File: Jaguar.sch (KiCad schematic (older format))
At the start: 26 parts, among them P1 12v-SW, P10 TPS, P11 TPS-GND, P12 O2, P13 O2-GND, P14 CRANK-IN, P15 CAM-IN, P16 GND, P17 GND2, P18 DIS-BYPASS, P19 IGN-ADVANCE, P2 12v-SW2, P20 PT3-5, P21 Inj-IN, P22 INJ-GND, P23 12v-SW4, P24 RELAY-GND, P25 FUEL-, P26 Injectors, P3 12v-SW3, P4 BRV-12v, P5 Ground, P6 IAT, P7 MAT, P8 COOLANT, P9 Ground

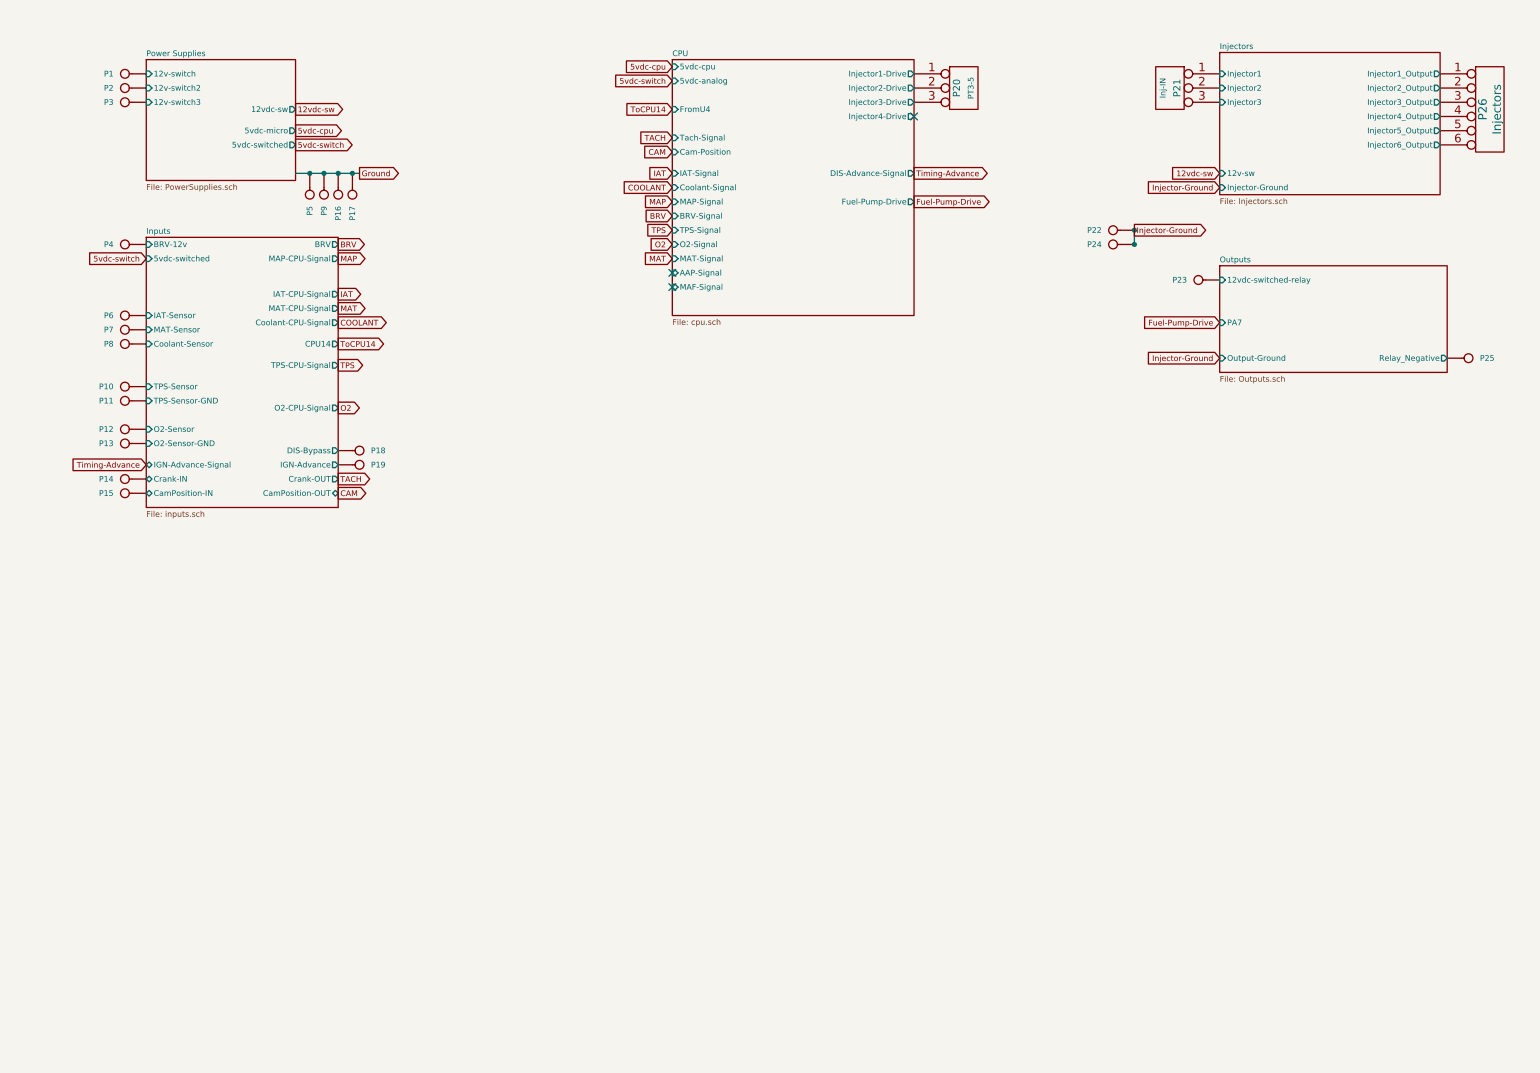
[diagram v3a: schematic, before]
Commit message: Improved schematic, re-design board, re-created PDF
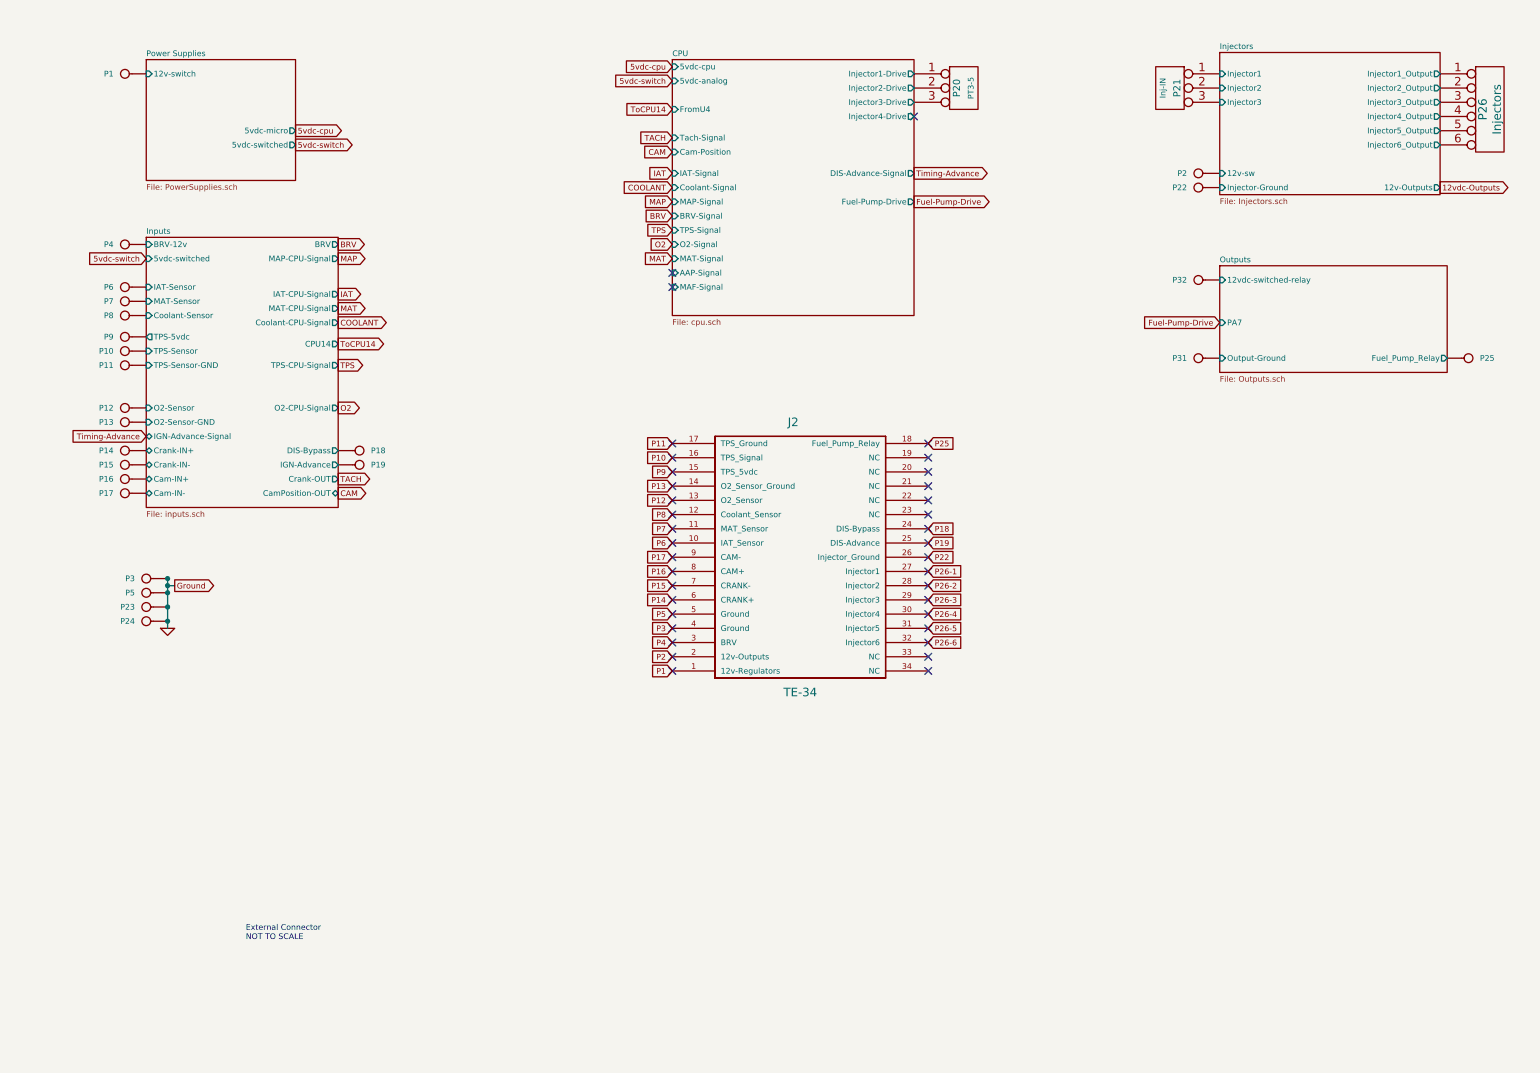
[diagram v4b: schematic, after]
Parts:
- added J2: TE-34, symbol TE-34
- added P31: OUT-GND, symbol CONN_1
- added P32: OUT-12v, symbol CONN_1
- P14: value CRANK-IN -> CRANK+
- P15: value CAM-IN -> CRANK-
- P16: value GND -> CAM+
- P17: value GND2 -> CAM-
- P23: value 12v-SW4 -> CRANK-GND
- P24: value RELAY-GND -> CAM-GND
- P3: value 12v-SW3 -> GND
- P5: value Ground -> GND2
- P9: value Ground -> TPS-5v
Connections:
- net labels added: 12vdc-Outputs, GND, P1, P10, P11, P12, P13, P14, P15, P16, P17, P18, P19, P2, P22, P25, P26-1, P26-2, P26-3, P26-4, P26-5, P26-6, P3, P4, P5, P6, P7, P8, P9
- net labels removed: 12vdc-sw, Injector-Ground
- no-connect marks 3 -> 37
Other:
- note added: "External Connector\nNOT TO SCALE"
- moved on the sheet: P10, P11, P12, P13, P14, P15, P16, P17, P2, P22, P3, P5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

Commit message: Fix MAX9926 Configuration and created new PCB and PDF
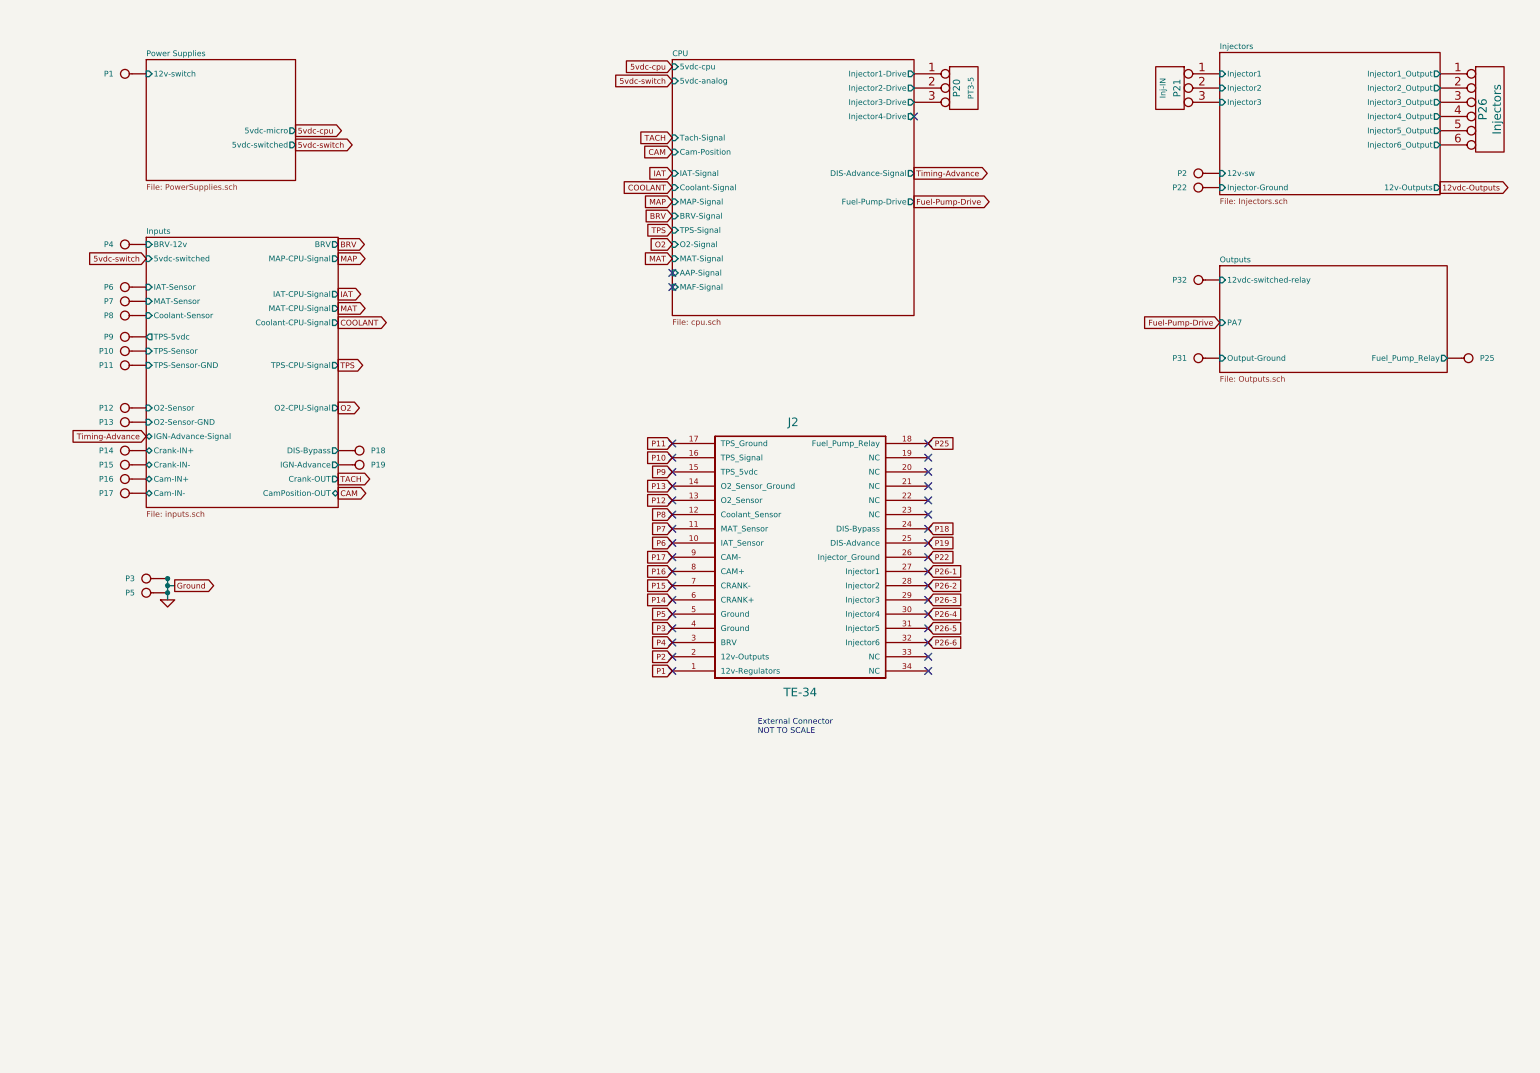
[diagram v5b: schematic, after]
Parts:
- removed P23: CRANK-GND, symbol CONN_1
- removed P24: CAM-GND, symbol CONN_1
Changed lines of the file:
@@
-EESchema Schematic File Version 2  date Mon 23 Jan 2012 07:28:42 AM EST
+EESchema Schematic File Version 2  date Mon 23 Jan 2012 01:49:16 PM EST
 LIBS:power
 LIBS:device
@@
 Comment4 ""
 $EndDescr
+Wire Wire Line
+	1650 4350 1650 4500
+Connection ~ 1650 4350
+Connection ~ 1650 4450
+Wire Wire Line
+	1700 4400 1650 4400
+Connection ~ 1650 4400
+$Sheet
+S 5200 700  1700 1800
+U 4F0A2F06
+F0 "CPU" 40
+F1 "cpu.sch" 40
+F2 "Fuel-Pump-Drive" O R 6900 1700 40
+F3 "Injector4-Drive" O R 6900 1100 40
+F4 "Injector3-Drive" O R 6900 1000 40
+F5 "Injector2-Drive" O R 6900 900 40
+F6 "Injector1-Drive" O R 6900 800 40
+F7 "DIS-Advance-Signal" O R 6900 1500 40
+F8 "Tach-Signal" I L 5200 1250 40
+F9 "MAF-Signal" I L 5200 2300 40
+F10 "MAT-Signal" I L 5200 2100 40
+F11 "BRV-Signal" I L 5200 1800 40
+F12 "MAP-Signal" I L 5200 1700 40
+F13 "O2-Signal" I L 5200 2000 40
+F14 "TPS-Signal" I L 5200 1900 40
+F15 "Coolant-Signal" I L 5200 1600 40
+F16 "IAT-Signal" I L 5200 1500 40
+F17 "AAP-Signal" I L 5200 2200 40
+F18 "Cam-Position" I L 5200 1350 40
+F19 "5vdc-analog" I L 5200 850 40
+F20 "5vdc-cpu" I L 5200 750 40
+$EndSheet
 $Comp
 L CONN_1 P32
@@
 F 1 "OUT-GND" H 8900 2855 30  0001 C CNN
 	1    8900 2800
-	-1   0    0    1
-$EndComp
-Connection ~ 1650 4650
-Connection ~ 1650 4550
-Wire Wire Line
-	1650 4700 1650 4350
-Connection ~ 1650 4400
-Wire Wire Line
-	1700 4400 1650 4400
-Connection ~ 1650 4450
-Connection ~ 1650 4350
-$Comp
-L CONN_1 P24
-U 1 1 4F1CCB30
-P 1500 4650
-F 0 "P24" H 1580 4650 40  0000 L CNN
-F 1 "CAM-GND" H 1500 4705 30  0001 C CNN
-	1    1500 4650
-	-1   0    0    1
-$EndComp
-$Comp
-L CONN_1 P23
-U 1 1 4F1CCB2B
-P 1500 4550
-F 0 "P23" H 1580 4550 40  0000 L CNN
-F 1 "CRANK-GND" H 1500 4605 30  0001 C CNN
-	1    1500 4550
 	-1   0    0    1
 $EndComp
@@
 L GND #PWR01
 U 1 1 4F1CCA54
-P 1650 4700
-F 0 "#PWR01" H 1650 4700 30  0001 C CNN
-F 1 "GND" H 1650 4630 30  0001 C CNN
-	1    1650 4700
+P 1650 4500
+F 0 "#PWR01" H 1650 4500 30  0001 C CNN
+F 1 "GND" H 1650 4430 30  0001 C CNN
+	1    1650 4500
 	1    0    0    -1
 $EndComp
@@
 Text GLabel 5200 5000 0    40   Input ~ 0
 P1
-Text Notes 2200 6900 0    40   ~ 0
+Text Notes 5800 5450 0    40   ~ 0
 External Connector\nNOT TO SCALE
 $Comp
@@
 F21 "CamPosition-OUT" B R 2850 3750 40
 F22 "Crank-OUT" O R 2850 3650 40
-F23 "CPU14" O R 2850 2700 40
-F24 "Cam-IN-" B L 1500 3750 40
-F25 "Crank-IN-" B L 1500 3550 40
-F26 "Cam-IN+" B L 1500 3650 40
-F27 "Crank-IN+" B L 1500 3450 40
-F28 "TPS-5vdc" O L 1500 2650 40
+F23 "Cam-IN-" B L 1500 3750 40
+F24 "Crank-IN-" B L 1500 3550 40
+F25 "Cam-IN+" B L 1500 3650 40
+F26 "Crank-IN+" B L 1500 3450 40
+F27 "TPS-5vdc" O L 1500 2650 40
 $EndSheet
 Text GLabel 1500 2100 0    40   Input ~ 0
@@
 5vdc-switch
 NoConn ~ 5200 2200
-Text GLabel 5200 1050 0    40   Input ~ 0
-ToCPU14
-Text GLabel 2850 2700 2    40   Output ~ 0
-ToCPU14
 $Comp
 L CONN_3 P21
@@
 	-1   0    0    1
 $EndComp
-$Sheet
-S 5200 700  1700 1800
-U 4F0A2F06
-F0 "CPU" 40
-F1 "cpu.sch" 40
-F2 "Fuel-Pump-Drive" O R 6900 1700 40
-F3 "Injector4-Drive" O R 6900 1100 40
-F4 "Injector3-Drive" O R 6900 1000 40
-F5 "Injector2-Drive" O R 6900 900 40
-F6 "Injector1-Drive" O R 6900 800 40
-F7 "DIS-Advance-Signal" O R 6900 1500 40
-F8 "Tach-Signal" I L 5200 1250 40
-F9 "MAF-Signal" I L 5200 2300 40
-F10 "MAT-Signal" I L 5200 2100 40
-F11 "BRV-Signal" I L 5200 1800 40
-F12 "MAP-Signal" I L 5200 1700 40
-F13 "O2-Signal" I L 5200 2000 40
-F14 "TPS-Signal" I L 5200 1900 40
-F15 "Coolant-Signal" I L 5200 1600 40
-F16 "IAT-Signal" I L 5200 1500 40
-F17 "AAP-Signal" I L 5200 2200 40
-F18 "Cam-Position" I L 5200 1350 40
-F19 "FromU4" I L 5200 1050 40
-F20 "5vdc-analog" I L 5200 850 40
-F21 "5vdc-cpu" I L 5200 750 40
-$EndSheet
 $EndSCHEMATC

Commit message: Updated Schematics and PDF, uploaded mc9s12xdp512 library
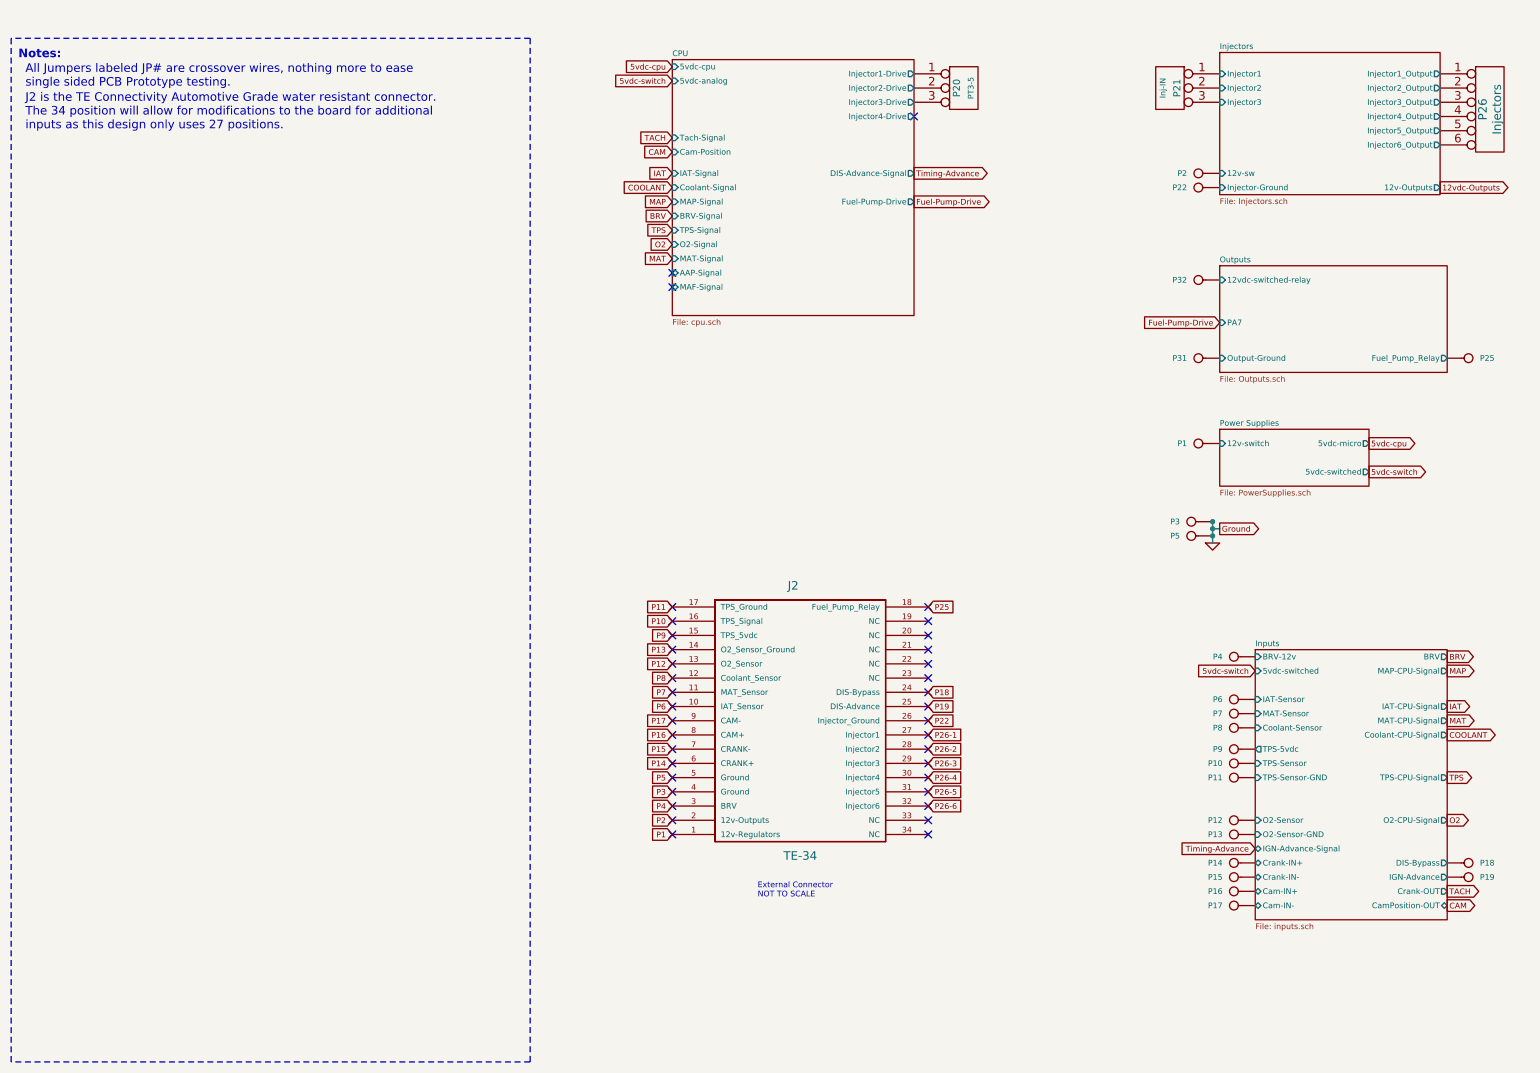
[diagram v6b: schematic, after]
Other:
- note added: "All Jumpers labeled JP# are crossover wires, nothing more to ease \nsingle sided PCB Prototype testing."
- note added: "J2 is the TE Connectivity Automotive Grade water resistant connector. \nThe 34 position will allow for modifications to the board for additional \ninputs as this design only uses 27 positions."
- note added: "Notes:"
- moved on the sheet: J2, P1, P10, P11, P12, P13, P14, P15, P16, P17, P18, P19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
